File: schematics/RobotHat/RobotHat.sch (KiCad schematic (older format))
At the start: 37 parts, among them J1 9Vin, J10 MotorB, J2 ICSP, J3 FTDI, J4 I2C, J5 3v3out, J6 AnalogPins, J7 WheelEncA, J8 WheelEncB, J9 MotorA, SW1 Reset, U1 ATmega328P-MU, U2 MIC5205-3.3YM5, U3 TB6612FNG, Y1 16MHz

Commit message: Dis
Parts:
- removed J5: 3v3out, Connector_JST:JST_XH_B2B-XH-A_1x02_P2.50mm_Vertical, symbol Connector_Generic:Conn_01x02
- removed U2: MIC5205-3.3YM5, Package_TO_SOT_SMD:SOT-23-5, symbol Regulator_Linear:MIC5205-3.3YM5
- added J5: Raspberry_Pi_2_3, Connector_PinSocket_2.54mm:PinSocket_2x20_P2.54mm_Vertical, symbol Connector:Raspberry_Pi_2_3
- added U2: MIC5205-5.0YM5, Package_TO_SOT_SMD:SOT-23-5, symbol Regulator_Linear:MIC5205-5.0YM5
- J2: value ICSP -> ATMega_ICSP
- J3: value FTDI -> ATMega_FTDI
- J6: value AnalogPins -> ATMega AnalogPins
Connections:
- net +3V3: now also J5.1 (3V3), J5.17 (3V3); no longer C5.1, C6.1, D1.2 (A)
- net +9V: now also U2.1 (IN), U2.3 (EN)
- net GND: now also J5.14 (GND), J5.20 (GND), J5.25 (GND), J5.30 (GND), J5.34 (GND), J5.39 (GND), J5.6 (GND), J5.9 (GND), U2.2 (GND)
- net SCL: now also J5.5 (SCL/GPIO3)
- net SDA: now also J5.3 (SDA/GPIO2)
- new net +5V: C5.1, C6.1, D1.2 (A), J5.2 (5V), J5.4 (5V), U2.5 (OUT)
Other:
- moved on the sheet: C10, C11, C8, C9, H1, H2, H3, H4, J10, J7, J8, J9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

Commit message: Added robot hat
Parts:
- added C12: 100uF, Capacitor_THT:CP_Radial_D5.0mm_P2.50mm, symbol Device:CP
- added C13: 220uf, Capacitor_THT:CP_Radial_D5.0mm_P2.50mm, symbol Device:CP
- added D3: 1N5822, Diode_THT:D_DO-201AD_P15.24mm_Horizontal, symbol Diode:1N5822
- added L1: 33uH, Inductor_THT:L_Radial_D8.7mm_P5.00mm_Fastron_07HCP, symbol Device:L
- added U4: LM2596S-5, Package_TO_SOT_SMD:TO-263-5_TabPin3, symbol Regulator_Switching:LM2596S-5
- H1, H2, H3, H4: footprint MountingHole:MountingHole_2.5mm -> MountingHole:MountingHole_2.7mm_M2.5_DIN965_Pad
- J6: footprint Connector_PinHeader_2.54mm:PinHeader_2x03_P2.54mm_Vertical -> Connector_PinSocket_2.54mm:PinSocket_2x03_P2.54mm_Vertical
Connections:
- net +5V: now also C13.1, L1.1, U4.4 (FB)
- net +9V: now also C12.1, U4.1 (VIN)
- net GND: now also C12.2, C13.2, D3.2 (A), U4.3 (GND), U4.5 (~ON~/OFF)
- new net: D3.1 (K), L1.2, U4.2 (OUT)
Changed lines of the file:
@@
 F 0 "H1" H 9650 996 50  0000 L CNN
 F 1 "MountingHole" H 9650 905 50  0000 L CNN
-F 2 "MountingHole:MountingHole_2.5mm" H 9550 950 50  0001 C CNN
+F 2 "MountingHole:MountingHole_2.7mm_M2.5_DIN965_Pad" H 9550 950 50  0001 C CNN
 F 3 "~" H 9550 950 50  0001 C CNN
 	1    9550 950
@@
 F 0 "H2" H 9650 1396 50  0000 L CNN
 F 1 "MountingHole" H 9650 1305 50  0000 L CNN
-F 2 "MountingHole:MountingHole_2.5mm" H 9550 1350 50  0001 C CNN
+F 2 "MountingHole:MountingHole_2.7mm_M2.5_DIN965_Pad" H 9550 1350 50  0001 C CNN
 F 3 "~" H 9550 1350 50  0001 C CNN
 	1    9550 1350
@@
 F 0 "H3" H 9650 1746 50  0000 L CNN
 F 1 "MountingHole" H 9650 1655 50  0000 L CNN
-F 2 "MountingHole:MountingHole_2.5mm" H 9550 1700 50  0001 C CNN
+F 2 "MountingHole:MountingHole_2.7mm_M2.5_DIN965_Pad" H 9550 1700 50  0001 C CNN
 F 3 "~" H 9550 1700 50  0001 C CNN
 	1    9550 1700
@@
 F 0 "H4" H 9650 2146 50  0000 L CNN
 F 1 "MountingHole" H 9650 2055 50  0000 L CNN
-F 2 "MountingHole:MountingHole_2.5mm" H 9550 2100 50  0001 C CNN
+F 2 "MountingHole:MountingHole_2.7mm_M2.5_DIN965_Pad" H 9550 2100 50  0001 C CNN
 F 3 "~" H 9550 2100 50  0001 C CNN
 	1    9550 2100
@@
 F 0 "J6" H 6000 7200 50  0000 C CNN
 F 1 "ATMega AnalogPins" H 6000 6750 50  0000 C CNN
-F 2 "Connector_PinHeader_2.54mm:PinHeader_2x03_P2.54mm_Vertical" H 5950 7000 50  0001 C CNN
+F 2 "Connector_PinSocket_2.54mm:PinSocket_2x03_P2.54mm_Vertical" H 5950 7000 50  0001 C CNN
 F 3 "~" H 5950 7000 50  0001 C CNN
 	1    5950 7000
@@
 Text GLabel 10450 3650 2    50   Input ~ 0
 SCL
+$Comp
+L Regulator_Switching:LM2596S-5 U4
+U 1 1 617ECBF6
+P 2300 -2650
+F 0 "U4" H 2300 -2283 50  0000 C CNN
+F 1 "LM2596S-5" H 2300 -2374 50  0000 C CNN
+F 2 "Package_TO_SOT_SMD:TO-263-5_TabPin3" H 2350 -2900 50  0001 L CIN
+F 3 "http://www.ti.com/lit/ds/symlink/lm2596.pdf" H 2300 -2650 50  0001 C CNN
+	1    2300 -2650
+	1    0    0    -1
+$EndComp
+$Comp
+L Device:CP C12
+U 1 1 617F2816
+P 1400 -2600
+F 0 "C12" H 1100 -2550 50  0000 L CNN
+F 1 "100uF" H 1050 -2650 50  0000 L CNN
+F 2 "Capacitor_THT:CP_Radial_D5.0mm_P2.50mm" H 1438 -2750 50  0001 C CNN
+F 3 "~" H 1400 -2600 50  0001 C CNN
+	1    1400 -2600
+	1    0    0    -1
+$EndComp
+$Comp
+L Diode:1N5822 D3
+U 1 1 617F7720
+P 3000 -2400
+F 0 "D3" V 3050 -2300 50  0000 L CNN
+F 1 "1N5822" V 3150 -2300 50  0000 L CNN
+F 2 "Diode_THT:D_DO-201AD_P15.24mm_Horizontal" H 3000 -2575 50  0001 C CNN
+F 3 "http://www.vishay.com/docs/88526/1n5820.pdf" H 3000 -2400 50  0001 C CNN
+	1    3000 -2400
+	0    1    1    0
+$EndComp
+$Comp
+L Device:L L1
+U 1 1 617FB4B7
+P 3350 -2550
+F 0 "L1" V 3250 -2550 50  0000 C CNN
+F 1 "33uH" V 3450 -2550 50  0000 C CNN
+F 2 "Inductor_THT:L_Radial_D8.7mm_P5.00mm_Fastron_07HCP" H 3350 -2550 50  0001 C CNN
+F 3 "~" H 3350 -2550 50  0001 C CNN
+	1    3350 -2550
+	0    1    1    0
+$EndComp
+$Comp
+L Device:CP C13
+U 1 1 617FDF61
+P 3750 -2400
+F 0 "C13" H 3868 -2354 50  0000 L CNN
+F 1 "220uf" H 3868 -2445 50  0000 L CNN
+F 2 "Capacitor_THT:CP_Radial_D5.0mm_P2.50mm" H 3788 -2550 50  0001 C CNN
+F 3 "~" H 3750 -2400 50  0001 C CNN
+	1    3750 -2400
+	1    0    0    -1
+$EndComp
+Wire Wire Line
+	2800 -2550 3000 -2550
+Wire Wire Line
+	3000 -2550 3200 -2550
+Connection ~ 3000 -2550
+Wire Wire Line
+	3500 -2550 3750 -2550
+Wire Wire Line
+	3750 -2550 4150 -2550
+Wire Wire Line
+	4150 -2550 4150 -2700
+Connection ~ 3750 -2550
+$Comp
+L power:+5V #PWR0108
+U 1 1 61810B8B
+P 4150 -2700
+F 0 "#PWR0108" H 4150 -2850 50  0001 C CNN
+F 1 "+5V" H 4165 -2527 50  0000 C CNN
+F 2 "" H 4150 -2700 50  0001 C CNN
+F 3 "" H 4150 -2700 50  0001 C CNN
+	1    4150 -2700
+	1    0    0    -1
+$EndComp
+Wire Wire Line
+	3750 -2550 3750 -2750
+Wire Wire Line
+	3750 -2750 2800 -2750
+Wire Wire Line
+	1100 -2750 1400 -2750
+Connection ~ 1400 -2750
+$Comp
+L power:GND #PWR0109
+U 1 1 6181C2EE
+P 2300 -2350
+F 0 "#PWR0109" H 2300 -2600 50  0001 C CNN
+F 1 "GND" H 2305 -2523 50  0000 C CNN
+F 2 "" H 2300 -2350 50  0001 C CNN
+F 3 "" H 2300 -2350 50  0001 C CNN
+	1    2300 -2350
+	1    0    0    -1
+$EndComp
+$Comp
+L power:GND #PWR0110
+U 1 1 6181C675
+P 3750 -2250
+F 0 "#PWR0110" H 3750 -2500 50  0001 C CNN
+F 1 "GND" H 3755 -2423 50  0000 C CNN
+F 2 "" H 3750 -2250 50  0001 C CNN
+F 3 "" H 3750 -2250 50  0001 C CNN
+	1    3750 -2250
+	1    0    0    -1
+$EndComp
+$Comp
+L power:GND #PWR0111
+U 1 1 6181CD38
+P 3000 -2250
+F 0 "#PWR0111" H 3000 -2500 50  0001 C CNN
+F 1 "GND" H 3005 -2423 50  0000 C CNN
+F 2 "" H 3000 -2250 50  0001 C CNN
+F 3 "" H 3000 -2250 50  0001 C CNN
+	1    3000 -2250
+	1    0    0    -1
+$EndComp
+$Comp
+L power:GND #PWR0112
+U 1 1 6181D33C
+P 1400 -2450
+F 0 "#PWR0112" H 1400 -2700 50  0001 C CNN
+F 1 "GND" H 1405 -2623 50  0000 C CNN
+F 2 "" H 1400 -2450 50  0001 C CNN
+F 3 "" H 1400 -2450 50  0001 C CNN
+	1    1400 -2450
+	1    0    0    -1
+$EndComp
+$Comp
+L power:+9V #PWR0113
+U 1 1 6181ECAE
+P 1100 -2750
+F 0 "#PWR0113" H 1100 -2900 50  0001 C CNN
+F 1 "+9V" H 1115 -2577 50  0000 C CNN
+F 2 "" H 1100 -2750 50  0001 C CNN
+F 3 "" H 1100 -2750 50  0001 C CNN
+	1    1100 -2750
+	1    0    0    -1
+$EndComp
+Wire Wire Line
+	1400 -2750 1800 -2750
+$Comp
+L power:GND #PWR0114
+U 1 1 61829011
+P 1750 -2350
+F 0 "#PWR0114" H 1750 -2600 50  0001 C CNN
+F 1 "GND" H 1755 -2523 50  0000 C CNN
+F 2 "" H 1750 -2350 50  0001 C CNN
+F 3 "" H 1750 -2350 50  0001 C CNN
+	1    1750 -2350
+	1    0    0    -1
+$EndComp
+Wire Wire Line
+	1800 -2550 1750 -2550
+Wire Wire Line
+	1750 -2550 1750 -2350
 $EndSCHEMATC

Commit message: Completed Robot Had for RaspberryPi
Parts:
- removed C1, C5: 10uF, Capacitor_SMD:CP_Elec_4x5.4, symbol Device:CP
- removed C6: 0.1uF, Capacitor_SMD:C_0402_1005Metric, symbol Device:C
- removed D1: RED, Diode_SMD:D_0402_1005Metric, symbol Device:LED
- removed R3: 10k, Resistor_SMD:R_0402_1005Metric, symbol Device:R
- removed U2: MIC5205-5.0YM5, Package_TO_SOT_SMD:SOT-23-5, symbol Regulator_Linear:MIC5205-5.0YM5
- added H5, H6: MountingHole, MountingHole:MountingHole_2.7mm_M2.5_DIN965_Pad, symbol Mechanical:MountingHole
- added J11: 5Vout, Connector_JST:JST_XH_B2B-XH-A_1x02_P2.50mm_Vertical, symbol Connector_Generic:Conn_01x02
- added J12: 3V3out, Connector_PinSocket_2.54mm:PinSocket_1x02_P2.54mm_Horizontal, symbol Connector_Generic:Conn_01x02
- C10, C9: footprint Capacitor_SMD:CP_Elec_4x5.4 -> Capacitor_THT:CP_Radial_D4.0mm_P2.00mm
- J6: footprint Connector_PinSocket_2.54mm:PinSocket_2x03_P2.54mm_Vertical -> Connector_PinSocket_2.54mm:PinSocket_2x03_P2.54mm_Horizontal
- R1, R2: footprint Resistor_SMD:R_0402_1005Metric -> Resistor_SMD:R_1206_3216Metric
- Y1: footprint Crystal:Crystal_SMD_HC49-SD -> Crystal:Resonator-2Pin_W7.0mm_H2.5mm
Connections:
- net +3V3: now also J12.2 (Pin_2)
- net +5V: now also J11.2 (Pin_2)
- net GND: now also J11.1 (Pin_1), J12.1 (Pin_1)
- no-connect marks 1 -> 0
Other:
- moved on the sheet: C12, C13, D3, L1, U4

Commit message: Re organizing
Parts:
- removed C9: 10uf, Capacitor_THT:CP_Radial_D4.0mm_P2.00mm, symbol Device:CP
- added C10, C9: 0.1uf, Capacitor_SMD:C_1206_3216Metric, symbol Device:C
- added D3: RED, Diode_SMD:D_0402_1005Metric, symbol Device:LED
- added R5: 330, Resistor_SMD:R_0402_1005Metric, symbol Device:R
- C11: footprint Capacitor_SMD:C_0402_1005Metric -> Capacitor_SMD:C_1206_3216Metric
- C7: renamed from C8; footprint Capacitor_SMD:C_0402_1005Metric -> Capacitor_SMD:C_1206_3216Metric
- D1: renamed from D3; value 1N5822 -> SS34; footprint Diode_THT:D_DO-201AD_P15.24mm_Horizontal -> RobotHat:SS34
- Y1: footprint Crystal:Resonator-2Pin_W7.0mm_H2.5mm -> Crystal:Crystal_HC49-4H_Vertical
- renumbered C12 to C1, C13 to C5, C7 to C6, C10 to C8, J9 to J10, J10 to J11, J5 to J12, J11 to J2, J12 to J3, J2 to J4, J3 to J5, J4 to J6, J6 to J7, J7 to J8, J8 to J9, R4 to R3, R5 to R4, U4 to U2
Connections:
- net +5V: now also R5.1
- net D10: now also U3.15 (PWMB); no longer U3.22 (AIN2)
- net D6: now also U3.22 (AIN2); no longer U3.15 (PWMB)
- net D7: now also U3.21 (AIN1); no longer U3.17 (BIN1)
- net D8: now also U3.17 (BIN1); no longer U3.16 (BIN2)
- net D9: now also U3.16 (BIN2); no longer U3.21 (AIN1)
- net GND: now also D3.1 (K)
- net MOTORA1: now also C9.1
- net MOTORA2: now also C9.2
- net MOTORB1: now also C10.1
- net MOTORB2: now also C10.2
- new net: D3.2 (A), R5.2
- no-connect marks 0 -> 26
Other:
- moved on the sheet: C7

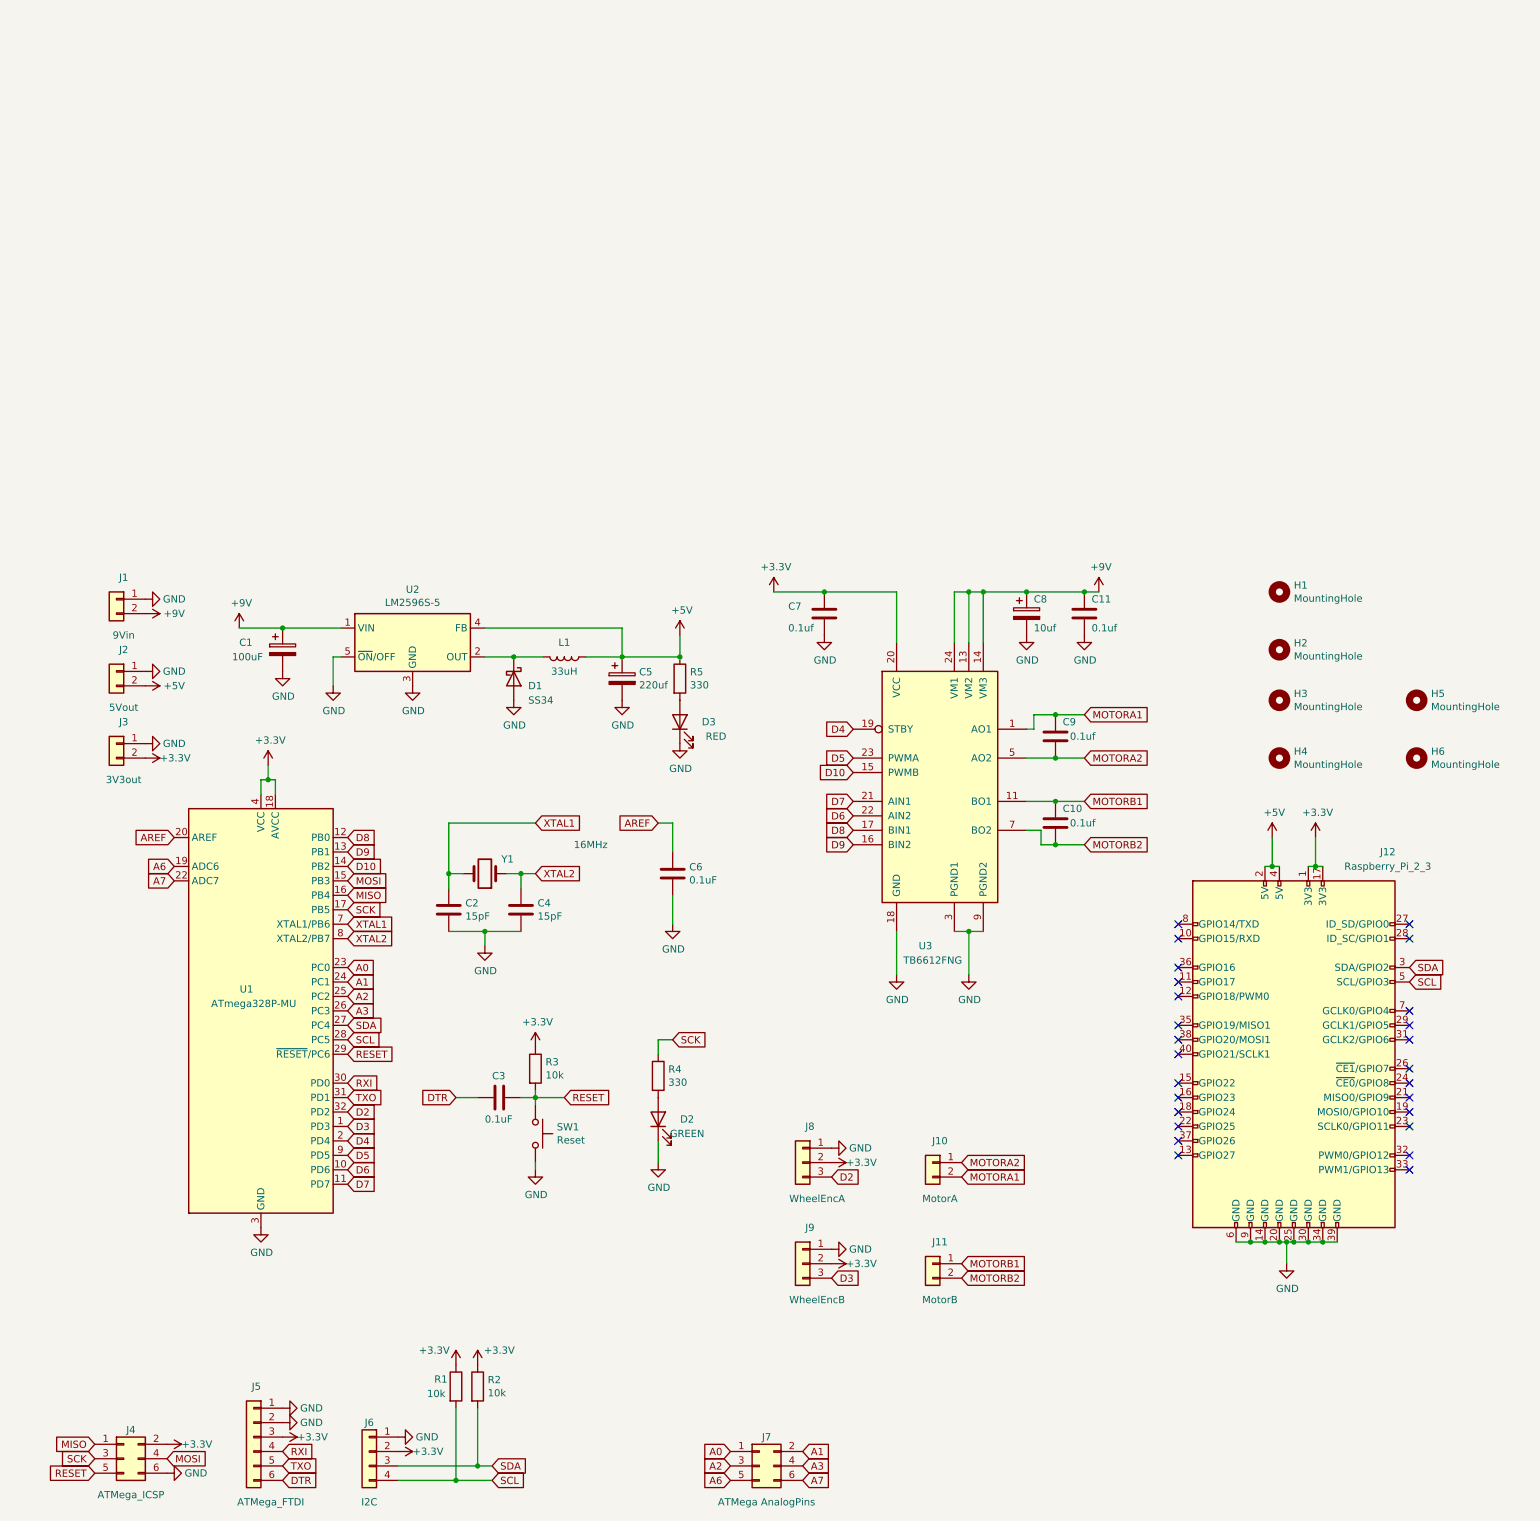
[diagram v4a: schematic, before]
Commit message: Arduino runs at 5v with logic level shifter on i2c bus
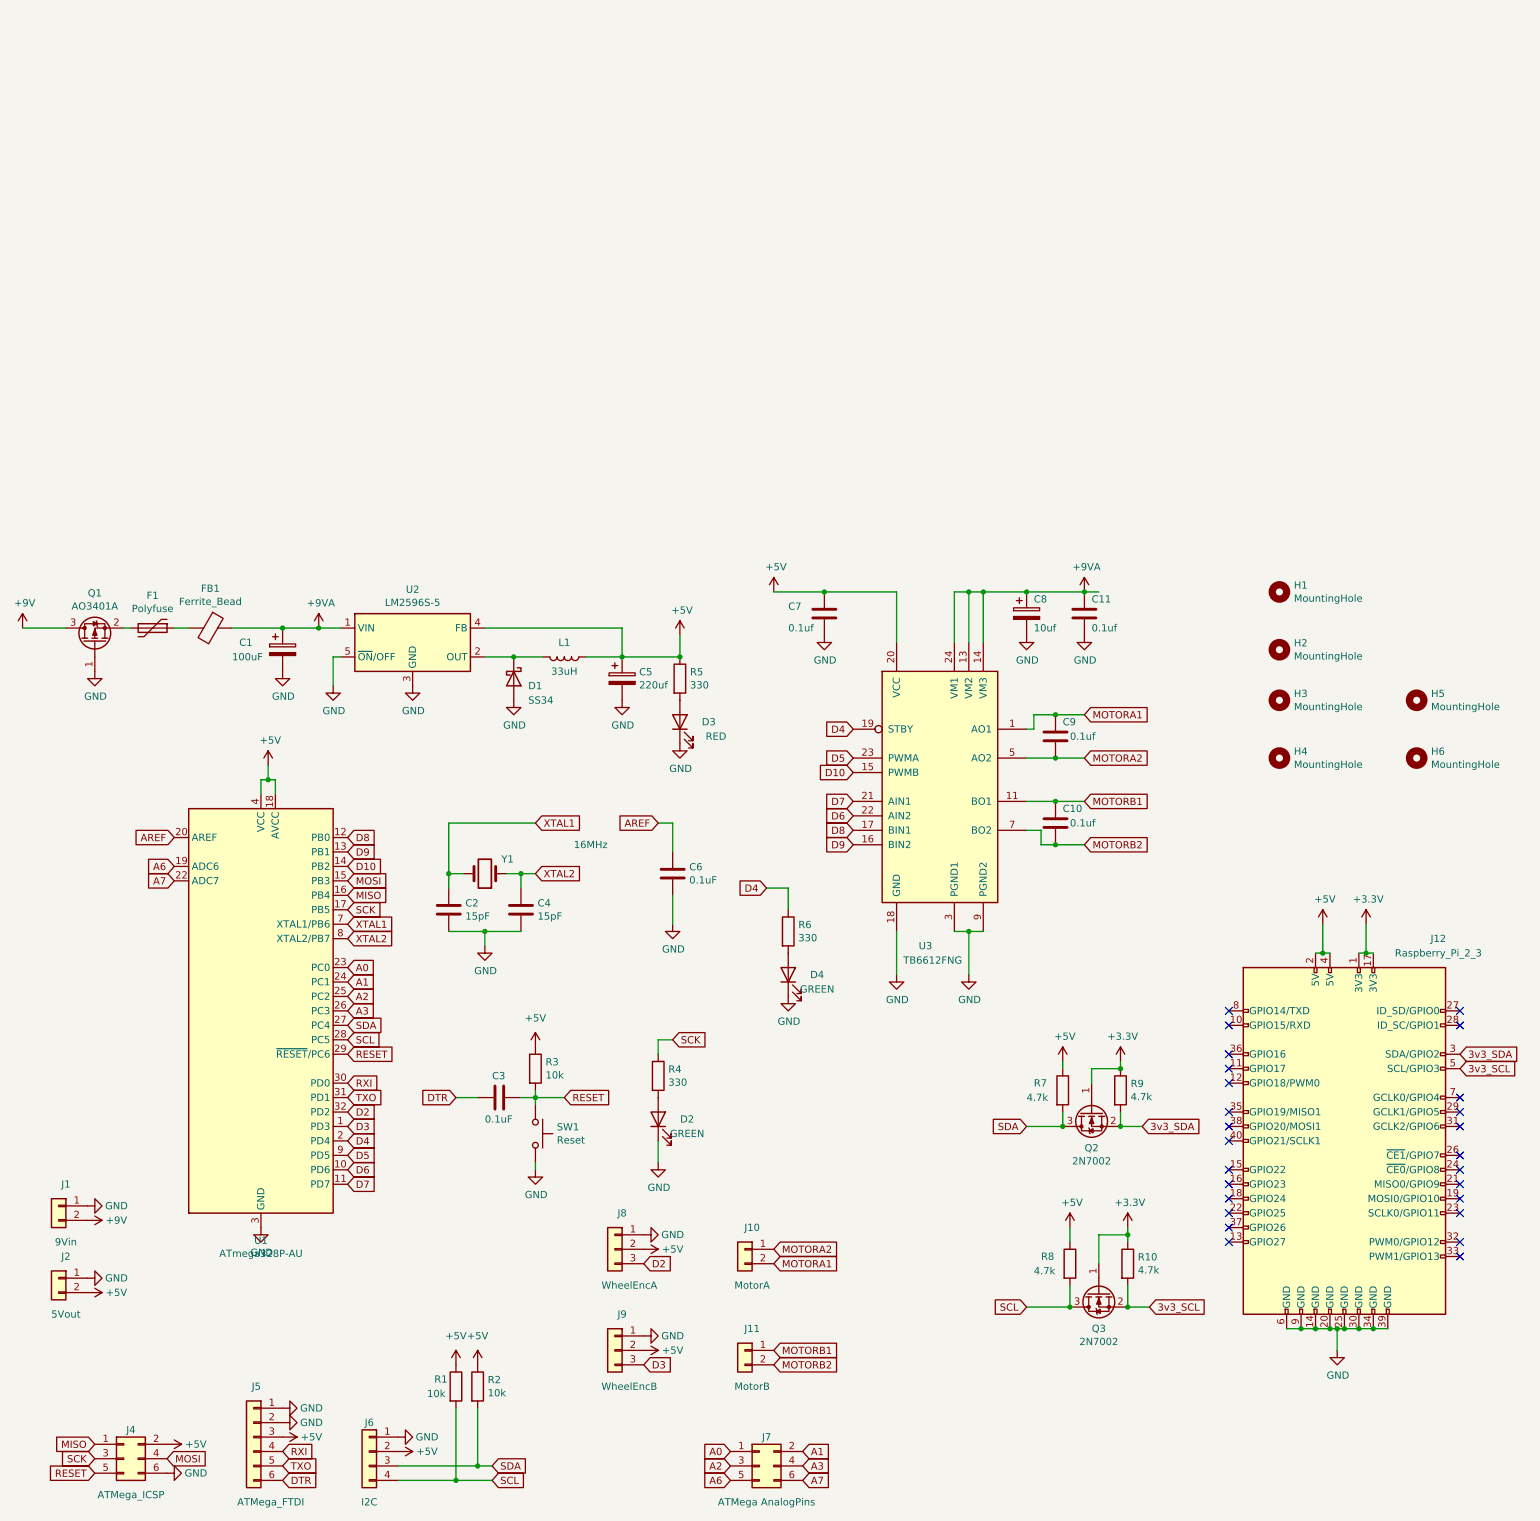
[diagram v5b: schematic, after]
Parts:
- removed J3: 3V3out, Connector_PinSocket_2.54mm:PinSocket_1x02_P2.54mm_Horizontal, symbol Connector_Generic:Conn_01x02
- removed U1: ATmega328P-MU, Package_DFN_QFN:QFN-32-1EP_5x5mm_P0.5mm_EP3.1x3.1mm, symbol MCU_Microchip_ATmega:ATmega328P-MU
- added D4: GREEN, Diode_SMD:D_0402_1005Metric, symbol Device:LED
- added F1: Polyfuse, Fuse:Fuse_1206_3216Metric, symbol Device:Polyfuse
- added FB1: Ferrite_Bead, Inductor_SMD:L_0805_2012Metric, symbol Device:Ferrite_Bead
- added Q1: AO3401A, Package_TO_SOT_SMD:SOT-23, symbol Transistor_FET:AO3401A
- added Q2, Q3: 2N7002, Package_TO_SOT_SMD:SOT-23, symbol Transistor_FET:2N7002
- added R10, R7, R8, R9: 4.7k, Resistor_SMD:R_0402_1005Metric, symbol Device:R
- added R6: 330, Resistor_SMD:R_0402_1005Metric, symbol Device:R
- added U1: ATmega328P-AU, Package_QFP:TQFP-32_7x7mm_P0.8mm, symbol MCU_Microchip_ATmega:ATmega328P-AU
- J5: footprint Connector_PinHeader_2.54mm:PinHeader_1x06_P2.54mm_Vertical -> Connector_PinHeader_2.54mm:PinHeader_1x06_P2.54mm_Horizontal
- J6: footprint Connector_JST:JST_XH_B4B-XH-A_1x04_P2.50mm_Vertical -> Connector_JST:JST_GH_BM04B-GHS-TBT_1x04-1MP_P1.25mm_Vertical
- SW1: footprint Button_Switch_SMD:SW_SPST_B3U-1000P-B -> Button_Switch_SMD:SW_Push_1P1T_NO_Vertical_Wuerth_434133025816
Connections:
- net +3V3: now also Q2.1 (G), Q3.1 (G), R10.1, R9.1; no longer C7.1, J4.2 (Pin_2), J5.3 (Pin_3), J6.2 (Pin_2), J8.2 (Pin_2), J9.2 (Pin_2), R1.1, R2.1, R3.1, U3.20 (VCC)
- net +5V: now also C7.1, J4.2 (Pin_2), J5.3 (Pin_3), J6.2 (Pin_2), J8.2 (Pin_2), J9.2 (Pin_2), R1.1, R2.1, R3.1, U3.20 (VCC), R7.1, R8.1, U1.18 (AVCC), U1.4 (VCC), U1.6 (VCC)
- net +9V: now also Q1.3 (D); no longer C1.1, C11.1, C8.1, U2.1 (VIN), U3.13 (VM2), U3.14 (VM3), U3.24 (VM1)
- net A0: now also U1.23 (PC0)
- net A1: now also U1.24 (PC1)
- net A2: now also U1.25 (PC2)
- net A3: now also U1.26 (PC3)
- net A6: now also U1.19 (ADC6)
- net A7: now also U1.22 (ADC7)
- net AREF: now also U1.20 (AREF)
- net D10: now also U1.14 (PB2)
- net D2: now also U1.32 (PD2)
- net D3: now also U1.1 (PD3)
- net D4: now also R6.1, U1.2 (PD4)
- net D5: now also U1.9 (PD5)
- net D6: now also U1.10 (PD6)
- net D7: now also U1.11 (PD7)
- net D8: now also U1.12 (PB0)
- net D9: now also U1.13 (PB1)
- net GND: now also D4.1 (K), Q1.1 (G), U1.21 (GND), U1.3 (GND), U1.5 (GND)
- net MISO: now also U1.16 (PB4)
- net MOSI: now also U1.15 (PB3)
- net RESET: now also U1.29 (~RESET~/PC6)
- net RXI: now also U1.30 (PD0)
- net SCK: now also U1.17 (PB5)
- net SCL: now also Q3.3 (D), R8.2, U1.28 (PC5); no longer J12.5 (SCL/GPIO3)
- net SDA: now also Q2.3 (D), R7.2, U1.27 (PC4); no longer J12.3 (SDA/GPIO2)
- net TXO: now also U1.31 (PD1)
- net XTAL1: now also U1.7 (XTAL1/PB6)
- net XTAL2: now also U1.8 (XTAL2/PB7)
- new net: D4.2 (A), R6.2
- new net: F1.2, Q1.2 (S)
- new net: F1.1, FB1.2
- new net +9VA: C1.1, C11.1, C8.1, FB1.1, U2.1 (VIN), U3.13 (VM2), U3.14 (VM3), U3.24 (VM1)
- new net 3v3_SCL: J12.5 (SCL/GPIO3), Q3.2 (S), R10.2
- new net 3v3_SDA: J12.3 (SDA/GPIO2), Q2.2 (S), R9.2
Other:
- moved on the sheet: J1, J10, J11, J12, J2, J8, J9
